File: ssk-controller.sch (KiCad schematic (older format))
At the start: 27 parts, among them J1 Conn_01x16, J2 Conn_01x08, J3 Conn_01x01, J4 USB_B, J5 Solenoid, Q1 Q_NMOS_GDS, SW1 SW_Push, U1 ATmega32U4-AU, U2 PRTR5V0U2X, Y1 16Mhz

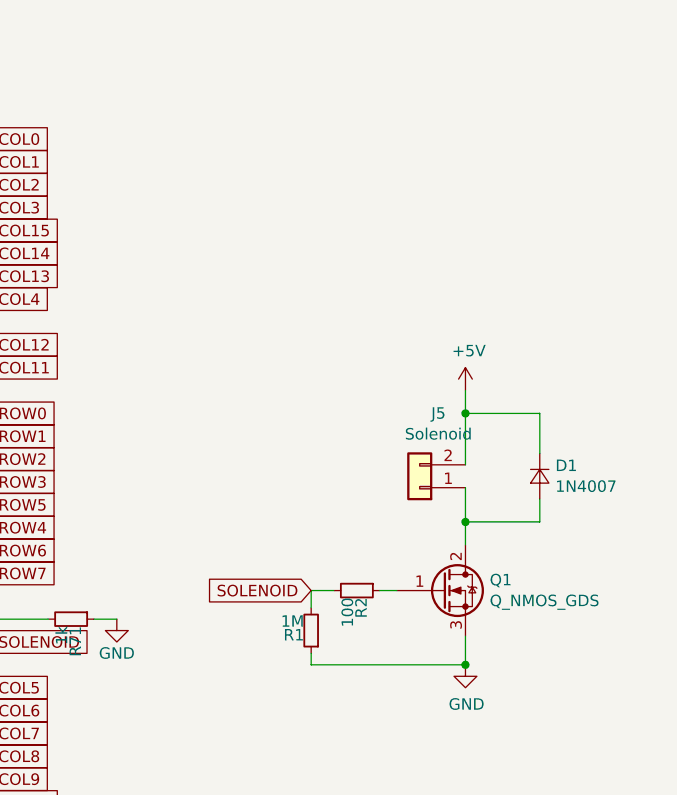
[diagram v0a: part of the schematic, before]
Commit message: Add both 9V and 5V solenoid compat
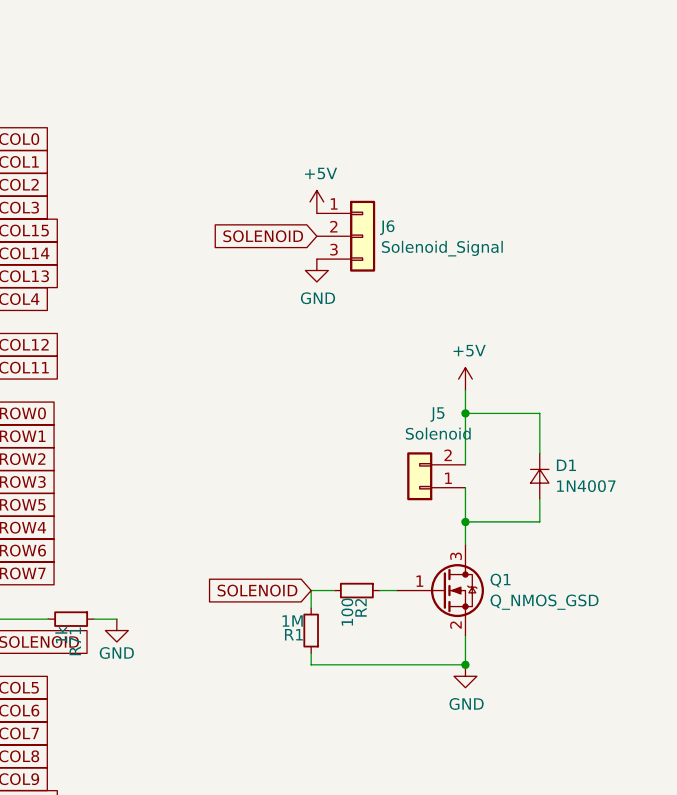
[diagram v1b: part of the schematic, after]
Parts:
- removed Q1: Q_NMOS_GDS, Package_TO_SOT_SMD:SOT-223-3_TabPin2, symbol Device:Q_NMOS_GDS
- added J6: Solenoid_Signal, random-keyboard-parts:JST-SR-3, symbol Connector_Generic:Conn_01x03
- added Q1: Q_NMOS_GSD, Package_TO_SOT_SMD:SOT-23, symbol Device:Q_NMOS_GSD
- D1: footprint Diode_SMD:D_SMA -> Diode_SMD:D_SOD-123
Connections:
- net +5V: now also J6.1 (Pin_1)
- net GND: now also J6.3 (Pin_3), Q1.2 (S)
- net SOLENOID: now also J6.2 (Pin_2)
- net at R2.1: now also Q1.1 (G)
- net at D1.2 (A), J5.1 (Pin_1): now also Q1.3 (D)
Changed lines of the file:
@@
-$EndComp
-$Comp
-L Device:Q_NMOS_GDS Q1
-U 1 1 5E7B6116
-P 10350 8875
-F 0 "Q1" H 10556 8921 50  0000 L CNN
-F 1 "Q_NMOS_GDS" H 10556 8830 50  0000 L CNN
-F 2 "Package_TO_SOT_SMD:SOT-223-3_TabPin2" H 10550 8975 50  0001 C CNN
-F 3 "~" H 10350 8875 50  0001 C CNN
-	1    10350 8875
-	1    0    0    -1
 $EndComp
 $Comp
@@
 F 0 "D1" V 10729 8443 50  0000 L CNN
 F 1 "1N4007" V 10820 8443 50  0000 L CNN
-F 2 "Diode_SMD:D_SMA" V 10775 8375 50  0001 C CNN
+F 2 "Diode_SMD:D_SOD-123" V 10775 8375 50  0001 C CNN
 F 3 "~" V 10775 8375 50  0001 C CNN
 	1    10775 8375
@@
 Connection ~ 850  9350
 $Comp
-L power:Earth #PWR?
+L power:Earth #PWR0105
 U 1 1 5E7F5B50
 P 10500 5900
-F 0 "#PWR?" H 10500 5650 50  0001 C CNN
+F 0 "#PWR0105" H 10500 5650 50  0001 C CNN
 F 1 "Earth" H 10500 5750 50  0001 C CNN
 F 2 "" H 10500 5900 50  0001 C CNN
@@
 	1    0    0    -1
 $EndComp
+$Comp
+L Device:Q_NMOS_GSD Q1
+U 1 1 5E825E71
+P 10350 8875
+F 0 "Q1" H 10556 8921 50  0000 L CNN
+F 1 "Q_NMOS_GSD" H 10556 8830 50  0000 L CNN
+F 2 "Package_TO_SOT_SMD:SOT-23" H 10550 8975 50  0001 C CNN
+F 3 "~" H 10350 8875 50  0001 C CNN
+	1    10350 8875
+	1    0    0    -1
+$EndComp
+Text GLabel 9800 7325 0    50   Input ~ 0
+SOLENOID
+$Comp
+L Connector_Generic:Conn_01x03 J6
+U 1 1 5E8364EE
+P 10000 7325
+F 0 "J6" H 10080 7367 50  0000 L CNN
+F 1 "Solenoid_Signal" H 10080 7276 50  0000 L CNN
+F 2 "random-keyboard-parts:JST-SR-3" H 10000 7325 50  0001 C CNN
+F 3 "~" H 10000 7325 50  0001 C CNN
+	1    10000 7325
+	1    0    0    -1
+$EndComp
+$Comp
+L power:+5V #PWR0110
+U 1 1 5E836E26
+P 9800 7225
+F 0 "#PWR0110" H 9800 7075 50  0001 C CNN
+F 1 "+5V" H 9815 7398 50  0000 C CNN
+F 2 "" H 9800 7225 50  0001 C CNN
+F 3 "" H 9800 7225 50  0001 C CNN
+	1    9800 7225
+	1    0    0    -1
+$EndComp
+$Comp
+L power:GND #PWR0111
+U 1 1 5E8375E6
+P 9800 7425
+F 0 "#PWR0111" H 9800 7175 50  0001 C CNN
+F 1 "GND" H 9805 7252 50  0000 C CNN
+F 2 "" H 9800 7425 50  0001 C CNN
+F 3 "" H 9800 7425 50  0001 C CNN
+	1    9800 7425
+	1    0    0    -1
+$EndComp

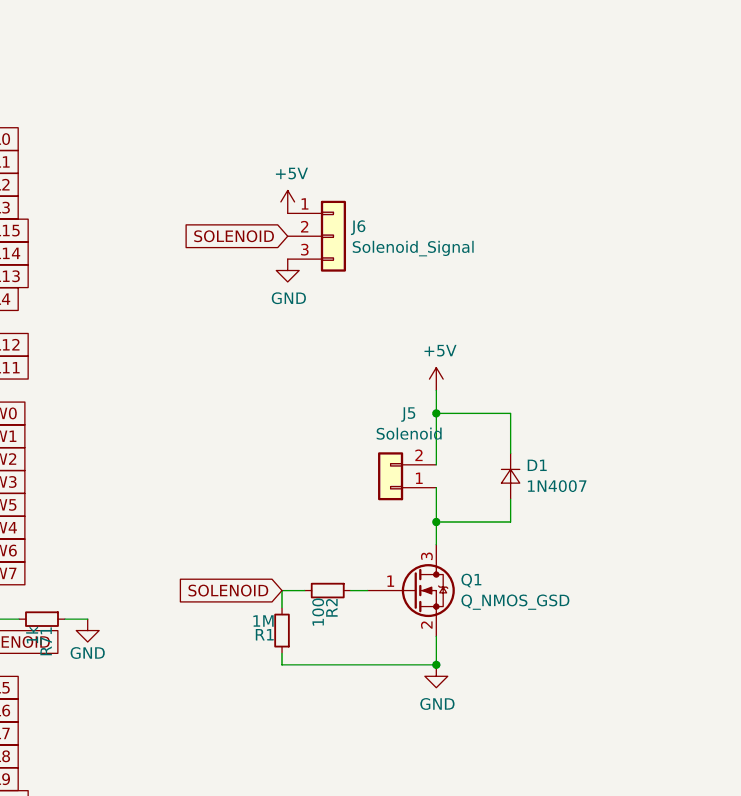
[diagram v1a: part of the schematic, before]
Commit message: Remove JST header, focus on 5V direct solenoid
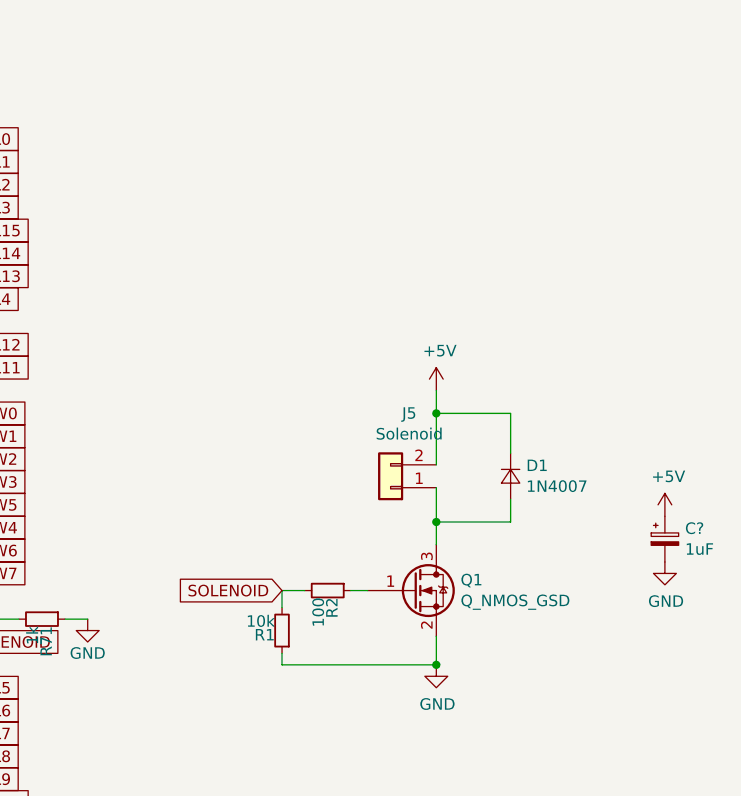
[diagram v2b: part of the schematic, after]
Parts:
- removed J6: Solenoid_Signal, random-keyboard-parts:JST-SR-3, symbol Connector_Generic:Conn_01x03
- added C?: 1uF, Capacitor_Tantalum_SMD:CP_EIA-3216-18_Kemet-A, symbol Device:CP_Small
- R1: value 1M -> 10k
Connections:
- net +5V: now also C?.1
- net GND: now also C?.2
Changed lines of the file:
@@
 P 9775 9050
 F 0 "R1" H 9805 9070 50  0000 L CNN
-F 1 "1M" H 9805 9010 50  0000 L CNN
+F 1 "10k" H 9805 9010 50  0000 L CNN
 F 2 "Resistor_SMD:R_0805_2012Metric" H 9775 9050 50  0001 C CNN
 F 3 "" H 9775 9050 50  0001 C CNN
@@
 	1    0    0    -1
 $EndComp
-Text GLabel 9800 7325 0    50   Input ~ 0
-SOLENOID
 $Comp
-L Connector_Generic:Conn_01x03 J6
-U 1 1 5E8364EE
-P 10000 7325
-F 0 "J6" H 10080 7367 50  0000 L CNN
-F 1 "Solenoid_Signal" H 10080 7276 50  0000 L CNN
-F 2 "random-keyboard-parts:JST-SR-3" H 10000 7325 50  0001 C CNN
-F 3 "~" H 10000 7325 50  0001 C CNN
-	1    10000 7325
+L Device:CP_Small C?
+U 1 1 5F73933F
+P 11450 8650
+F 0 "C?" H 11538 8696 50  0000 L CNN
+F 1 "1uF" H 11538 8605 50  0000 L CNN
+F 2 "Capacitor_Tantalum_SMD:CP_EIA-3216-18_Kemet-A" H 11450 8650 50  0001 C CNN
+F 3 "~" H 11450 8650 50  0001 C CNN
+	1    11450 8650
 	1    0    0    -1
 $EndComp
 $Comp
-L power:+5V #PWR0110
-U 1 1 5E836E26
-P 9800 7225
-F 0 "#PWR0110" H 9800 7075 50  0001 C CNN
-F 1 "+5V" H 9815 7398 50  0000 C CNN
-F 2 "" H 9800 7225 50  0001 C CNN
-F 3 "" H 9800 7225 50  0001 C CNN
-	1    9800 7225
+L power:+5V #PWR?
+U 1 1 5F739CAA
+P 11450 8550
+F 0 "#PWR?" H 11450 8400 50  0001 C CNN
+F 1 "+5V" H 11465 8723 50  0000 C CNN
+F 2 "" H 11450 8550 50  0001 C CNN
+F 3 "" H 11450 8550 50  0001 C CNN
+	1    11450 8550
 	1    0    0    -1
 $EndComp
 $Comp
-L power:GND #PWR0111
-U 1 1 5E8375E6
-P 9800 7425
-F 0 "#PWR0111" H 9800 7175 50  0001 C CNN
-F 1 "GND" H 9805 7252 50  0000 C CNN
-F 2 "" H 9800 7425 50  0001 C CNN
-F 3 "" H 9800 7425 50  0001 C CNN
-	1    9800 7425
+L power:GND #PWR?
+U 1 1 5F73A51F
+P 11450 8750
+F 0 "#PWR?" H 11450 8500 50  0001 C CNN
+F 1 "GND" H 11455 8577 50  0000 C CNN
+F 2 "" H 11450 8750 50  0001 C CNN
+F 3 "" H 11450 8750 50  0001 C CNN
+	1    11450 8750
 	1    0    0    -1
 $EndComp

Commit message: Update to r2.2
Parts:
- gave numbers to parts that had none: 1
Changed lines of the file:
@@
 $EndComp
 $Comp
-L Device:CP_Small C?
+L Device:CP_Small C9
 U 1 1 5F73933F
 P 11450 8650
-F 0 "C?" H 11538 8696 50  0000 L CNN
+F 0 "C9" H 11538 8696 50  0000 L CNN
 F 1 "1uF" H 11538 8605 50  0000 L CNN
 F 2 "Capacitor_Tantalum_SMD:CP_EIA-3216-18_Kemet-A" H 11450 8650 50  0001 C CNN
@@
 $EndComp
 $Comp
-L power:+5V #PWR?
+L power:+5V #PWR0110
 U 1 1 5F739CAA
 P 11450 8550
-F 0 "#PWR?" H 11450 8400 50  0001 C CNN
+F 0 "#PWR0110" H 11450 8400 50  0001 C CNN
 F 1 "+5V" H 11465 8723 50  0000 C CNN
 F 2 "" H 11450 8550 50  0001 C CNN
@@
 $EndComp
 $Comp
-L power:GND #PWR?
+L power:GND #PWR0111
 U 1 1 5F73A51F
 P 11450 8750
-F 0 "#PWR?" H 11450 8500 50  0001 C CNN
+F 0 "#PWR0111" H 11450 8500 50  0001 C CNN
 F 1 "GND" H 11455 8577 50  0000 C CNN
 F 2 "" H 11450 8750 50  0001 C CNN
